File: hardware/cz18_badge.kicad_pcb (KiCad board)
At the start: 2 copper layers, 91.5 x 99.6 mm, 37 parts, among them J1 Dev breakout (opt.), J2 VCC (max 5V), J3 GND, J4 LEDS OUT, SW1 MODE, SW2 SLOT, SW3 LEARN, SW4 PLAY, U1 CHQ1838, U2 NRF24L01 (opt.)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

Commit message: Finished annotation
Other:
- board text added: "D2"
- board text added: "D3"
- board text added: "D4"
- board text added: "D5"
- board text added: "D6"
- board text added: "RX"
- board text added: "TX"
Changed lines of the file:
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@@
     (links 119)
     (no_connects 119)
-    (area 86.149249 48.166589 177.749413 147.831598)
+    (area 79.807143 32.561796 178.694531 147.831598)
     (thickness 1.6)
-    (drawings 421)
+    (drawings 430)
     (tracks 0)
     (zones 0)
@@
     (35 F.Paste user)
     (36 B.SilkS user)
-    (37 F.SilkS user)
+    (37 F.SilkS user hide)
     (38 B.Mask user)
     (39 F.Mask user)
@@
     (pad 1 thru_hole circle (at 2.280419 -2.280419) (size 0.9 0.9) (drill 0.6) (layers *.Cu *.Mask))
   )
+  (gr_text TX (at 169.5 86.5 10) (layer B.SilkS)
+    (effects (font (size 1 1) (thickness 0.15)) (justify mirror))
+  )
+  (gr_text RX (at 170 89 10) (layer B.SilkS)
+    (effects (font (size 1 1) (thickness 0.15)) (justify mirror))
+  )
+  (gr_text RST (at 170.5 91.5 10) (layer B.SilkS)
+    (effects (font (size 1 1) (thickness 0.15)) (justify mirror))
+  )
+  (gr_text GND (at 171 94 10) (layer B.SilkS)
+    (effects (font (size 1 1) (thickness 0.15)) (justify mirror))
+  )
+  (gr_text D2 (at 171 96.5 10) (layer B.SilkS)
+    (effects (font (size 1 1) (thickness 0.15)) (justify mirror))
+  )
+  (gr_text D3 (at 171.5 99 10) (layer B.SilkS)
+    (effects (font (size 1 1) (thickness 0.15)) (justify mirror))
+  )
+  (gr_text D4 (at 172 101.5 10) (layer B.SilkS)
+    (effects (font (size 1 1) (thickness 0.15)) (justify mirror))
+  )
+  (gr_text D5 (at 172.5 104 10) (layer B.SilkS)
+    (effects (font (size 1 1) (thickness 0.15)) (justify mirror))
+  )
+  (gr_text D6 (at 173 106.5 10) (layer B.SilkS)
+    (effects (font (size 1 1) (thickness 0.15)) (justify mirror))
+  )
   (gr_text D7 (at 173.5 109 10) (layer B.SilkS)

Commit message: Added minimal track widths and clearances for JLCPCB
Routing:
- added copper zone on B.Cu, net VCC
- added copper zone on F.Cu, net VCC
- removed copper zone on B.Cu, net GND
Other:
- net class Default: clearance 0.25 -> 0.127; trace_width 0.25 -> 0.127
- net class Power added: clearance 0.25, trace_width 0.25, via_dia 0.6, via_drill 0.4
- rule trace_clearance: 0.25 -> 0.127
- rule trace_min: 0.2 -> 0.127
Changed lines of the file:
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@@
     (35 F.Paste user)
     (36 B.SilkS user)
-    (37 F.SilkS user hide)
+    (37 F.SilkS user)
     (38 B.Mask user)
     (39 F.Mask user)
@@
   )
   (setup
-    (last_trace_width 0.25)
-    (trace_clearance 0.25)
-    (zone_clearance 0.508)
+    (last_trace_width 0.127)
+    (trace_clearance 0.127)
+    (zone_clearance 0.2)
     (zone_45_only no)
-    (trace_min 0.2)
+    (trace_min 0.127)
     (segment_width 0.25)
     (edge_width 0.15)
@@
   (net 34 "Net-(U2-Pad8)")
   (net_class Default "This is the default net class."
-    (clearance 0.25)
-    (trace_width 0.25)
+    (clearance 0.127)
+    (trace_width 0.127)
     (via_dia 0.6)
     (via_drill 0.4)
     (uvia_dia 0.3)
     (uvia_drill 0.1)
-    (add_net 3V3)
     (add_net A0)
     (add_net A1)
@@
     (add_net A6)
     (add_net A7)
-    (add_net AREF)
     (add_net BUZZ1)
     (add_net BUZZ2)
@@
     (add_net D7)
     (add_net D8)
-    (add_net GND)
     (add_net "Net-(D1-Pad4)")
     (add_net "Net-(D2-Pad4)")
@@
     (add_net RX)
     (add_net TX)
+  )
+  (net_class Power ""
+    (clearance 0.25)
+    (trace_width 0.25)
+    (via_dia 0.6)
+    (via_drill 0.4)
+    (uvia_dia 0.3)
+    (uvia_drill 0.1)
+    (add_net 3V3)
+    (add_net AREF)
+    (add_net GND)
     (add_net VCC)
     (add_net VIN)
@@
   (gr_line (start 164.777843 140.94158) (end 161.054639 143.439932) (layer Edge.Cuts) (width 0.1))
   (gr_line (start 166.819753 139.21182) (end 164.777843 140.94158) (layer Edge.Cuts) (width 0.1))
-  (zone (net 15) (net_name GND) (layer F.Cu) (hatch full 0.508)
+  (zone (net 3) (net_name VCC) (layer F.Cu) (hatch full 0.508)
     (connect_pads (clearance 0.808))
     (min_thickness 0.254)
@@
     )
   )
-  (zone (net 15) (net_name GND) (layer F.Cu) (hatch full 0.508)
+  (zone (net 3) (net_name VCC) (layer F.Cu) (hatch full 0.508)
     (connect_pads (clearance 0.808))
     (min_thickness 0.254)
@@
     )
   )
-  (zone (net 15) (net_name GND) (layer F.Cu) (hatch full 0.508)
+  (zone (net 3) (net_name VCC) (layer F.Cu) (hatch full 0.508)
     (connect_pads (clearance 0.808))
     (min_thickness 0.254)
@@
     )
   )
-  (zone (net 15) (net_name GND) (layer F.Cu) (hatch full 0.508)
+  (zone (net 3) (net_name VCC) (layer F.Cu) (hatch full 0.508)
     (connect_pads (clearance 0.808))
     (min_thickness 0.254)
@@
     )
   )
-  (zone (net 15) (net_name GND) (layer F.Cu) (hatch full 0.508)
-    (connect_pads (clearance 0.808))
-    (min_thickness 0.254)
-    (fill (arc_segments 16) (thermal_gap 0.508) (thermal_bridge_width 0.508))
+  (zone (net 3) (net_name VCC) (layer F.Cu) (hatch full 0.508)
+    (connect_pads (clearance 0.2))
+    (min_thickness 0.127)
+    (fill (arc_segments 16) (thermal_gap 0.2) (thermal_bridge_width 0.508))
     (polygon
       (pts
@@
     )
   )
-  (zone (net 15) (net_name GND) (layer F.Cu) (hatch full 0.508)
-    (connect_pads (clearance 0.508))
-    (min_thickness 0.254)
-    (fill (arc_segments 16) (thermal_gap 0.508) (thermal_bridge_width 0.508))
+  (zone (net 3) (net_name VCC) (layer F.Cu) (hatch full 0.508)
+    (connect_pads (clearance 0.2))
+    (min_thickness 0.127)
+    (fill (arc_segments 16) (thermal_gap 0.2) (thermal_bridge_width 0.508))
     (polygon
       (pts
@@
     )
   )
-  (zone (net 15) (net_name GND) (layer F.Cu) (hatch full 0.508)
-    (connect_pads (clearance 0.508))
-    (min_thickness 0.254)
-    (fill (arc_segments 16) (thermal_gap 0.508) (thermal_bridge_width 0.508))
+  (zone (net 3) (net_name VCC) (layer F.Cu) (hatch full 0.508)
+    (connect_pads (clearance 0.2))
+    (min_thickness 0.127)
+    (fill (arc_segments 16) (thermal_gap 0.2) (thermal_bridge_width 0.508))
     (polygon
       (pts
@@
     )
   )
-  (zone (net 15) (net_name GND) (layer F.Cu) (hatch full 0.508)
-    (connect_pads (clearance 0.508))
-    (min_thickness 0.254)
-    (fill (arc_segments 16) (thermal_gap 0.508) (thermal_bridge_width 0.508))
+  (zone (net 3) (net_name VCC) (layer F.Cu) (hatch full 0.508)
+    (connect_pads (clearance 0.2))
+    (min_thickness 0.127)
+    (fill (arc_segments 16) (thermal_gap 0.2) (thermal_bridge_width 0.508))
     (polygon
       (pts
@@
     )
   )
-  (zone (net 15) (net_name GND) (layer F.Cu) (hatch full 0.508)
-    (connect_pads (clearance 0.508))
-    (min_thickness 0.254)
-    (fill (arc_segments 16) (thermal_gap 0.508) (thermal_bridge_width 0.508))
+  (zone (net 3) (net_name VCC) (layer F.Cu) (hatch full 0.508)
+    (connect_pads (clearance 0.2))
+    (min_thickness 0.127)
+    (fill (arc_segments 16) (thermal_gap 0.2) (thermal_bridge_width 0.508))
     (polygon
       (pts
@@
     )
   )
-  (zone (net 15) (net_name GND) (layer F.Cu) (hatch full 0.508)
-    (connect_pads (clearance 0.808))
-    (min_thickness 0.254)
-    (fill (arc_segments 16) (thermal_gap 0.508) (thermal_bridge_width 0.508))
+  (zone (net 3) (net_name VCC) (layer F.Cu) (hatch full 0.508)
+    (connect_pads (clearance 0.2))
+    (min_thickness 0.127)
+    (fill (arc_segments 16) (thermal_gap 0.2) (thermal_bridge_width 0.508))
     (polygon
       (pts
@@
     )
   )
-  (zone (net 15) (net_name GND) (layer F.Cu) (hatch full 0.508)
-    (connect_pads (clearance 0.808))
-    (min_thickness 0.254)
-    (fill (arc_segments 16) (thermal_gap 0.508) (thermal_bridge_width 0.508))
+  (zone (net 3) (net_name VCC) (layer F.Cu) (hatch full 0.508)
+    (connect_pads (clearance 0.2))
+    (min_thickness 0.127)
+    (fill (arc_segments 16) (thermal_gap 0.2) (thermal_bridge_width 0.508))
     (polygon
       (pts
@@
   )
   (zone (net 15) (net_name GND) (layer F.Cu) (hatch full 0.508)
-    (connect_pads (clearance 0.808))
-    (min_thickness 0.254)
-    (fill (arc_segments 16) (thermal_gap 0.508) (thermal_bridge_width 0.508))
+    (connect_pads (clearance 0.2))
+    (min_thickness 0.127)
+    (fill (arc_segments 16) (thermal_gap 0.2) (thermal_bridge_width 0.508))
     (polygon
       (pts
@@
     )
   )
-  (zone (net 15) (net_name GND) (layer F.Cu) (hatch full 0.508)
-    (connect_pads (clearance 0.808))
-    (min_thickness 0.254)
-    (fill (arc_segments 16) (thermal_gap 0.508) (thermal_bridge_width 0.508))
+  (zone (net 3) (net_name VCC) (layer F.Cu) (hatch full 0.508)
+    (connect_pads (clearance 0.2))
+    (min_thickness 0.127)
+    (fill (arc_segments 16) (thermal_gap 0.2) (thermal_bridge_width 0.508))
     (polygon
       (pts
@@
     )
   )
-  (zone (net 15) (net_name GND) (layer B.Cu) (hatch full 0.508)
-    (connect_pads (clearance 0.508))
-    (min_thickness 0.254)
-    (fill (arc_segments 16) (thermal_gap 0.508) (thermal_bridge_width 0.508))
+  (zone (net 3) (net_name VCC) (layer B.Cu) (hatch full 0.508)
+    (connect_pads (clearance 0.2))
+    (min_thickness 0.127)
+    (fill (arc_segments 16) (thermal_gap 0.2) (thermal_bridge_width 0.508))
     (polygon
       (pts

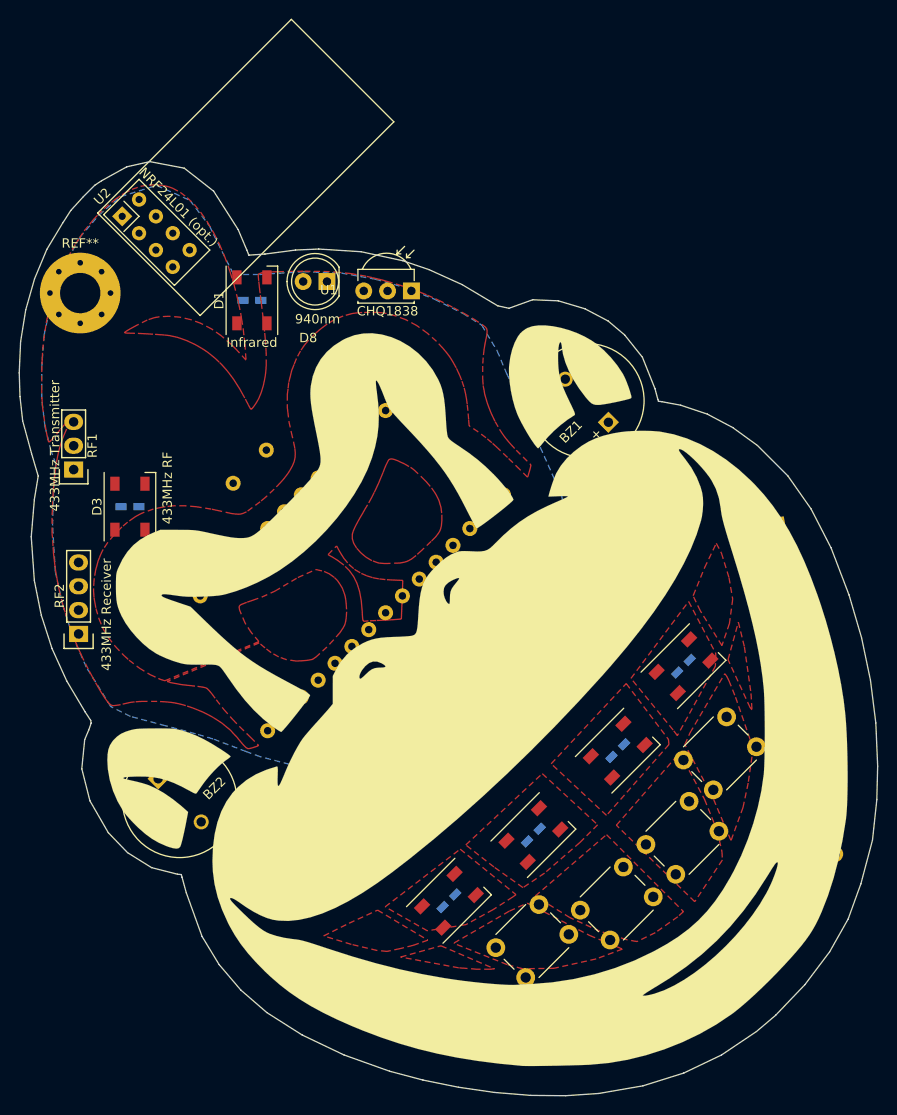
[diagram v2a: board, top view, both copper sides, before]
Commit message: Performed Autoroute, still 14 connections missing.
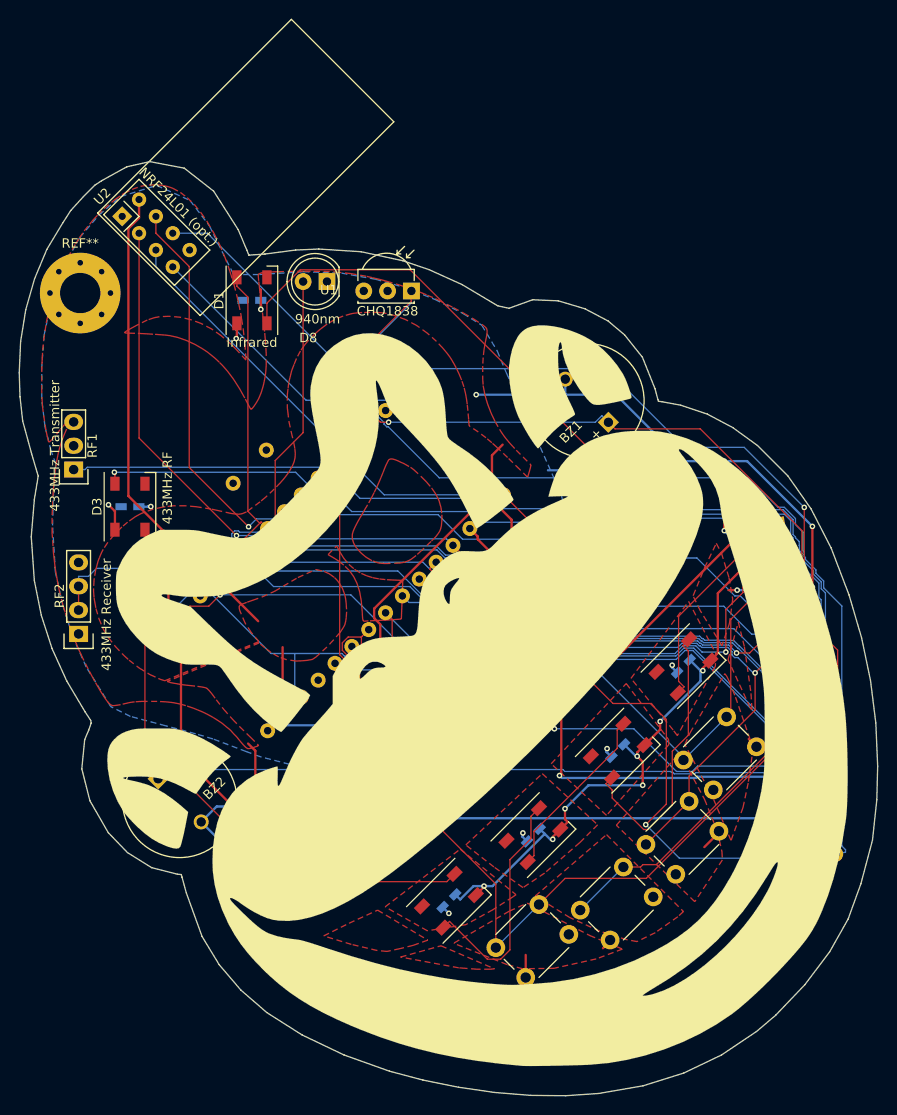
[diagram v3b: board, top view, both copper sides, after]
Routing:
- net GND: track 0.00 -> 196.3 mm, vias 0 -> 17
- net 3V3: track 0.00 -> 185.4 mm
- net D11: track 0.00 -> 122.6 mm, vias 0 -> 1
- net A0: track 0.00 -> 121.0 mm, vias 0 -> 2
- net D12: track 0.00 -> 120.5 mm
- net D13: track 0.00 -> 114.3 mm, vias 0 -> 1
- net BUZZ2: track 0.00 -> 114.2 mm, vias 0 -> 1
- net A1: track 0.00 -> 110.9 mm, vias 0 -> 2
- net D7: track 0.00 -> 109.6 mm
- net D8: track 0.00 -> 108.2 mm
- net D4: track 0.00 -> 97.8 mm, vias 0 -> 1
- net D3: track 0.00 -> 94.7 mm
- net BUZZ1: track 0.00 -> 87.8 mm, vias 0 -> 1
- net A5: track 0.00 -> 86.9 mm, vias 0 -> 1
- net D2: track 0.00 -> 85.3 mm, vias 0 -> 1
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
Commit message: Completed final manual routing
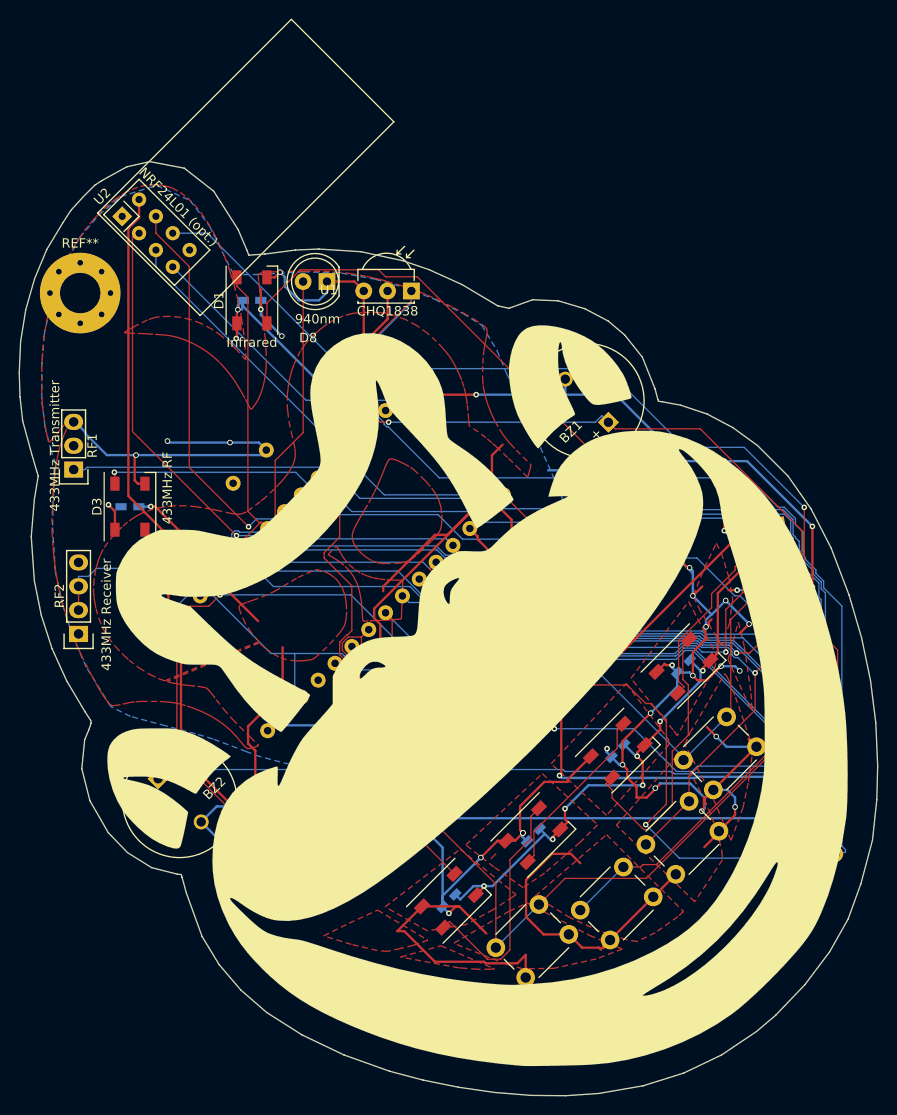
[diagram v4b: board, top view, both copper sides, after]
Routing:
- net VCC: track 36.0 -> 283.2 mm, vias 8 -> 28
- net GND: track 196.3 -> 292.9 mm, vias 17 -> 24
- net 3V3: track 185.4 -> 197.8 mm
- net Net-(D3-Pad4): track 62.1 -> 67.0 mm
- net BUZZ2: track 114.2 -> 116.7 mm
- net A1: track 110.9 -> 111.7 mm
- net (no net): track 0.00 -> 0.71 mm
- added copper zone on F.Cu, net 3V3

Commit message: Added eye shade fill zones again, and performed final modifications to tracks. Generated gerber files.
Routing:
- net GND: track 292.9 -> 318.1 mm
- net VCC: track 283.2 -> 294.4 mm
- net 3V3: track 197.8 -> 188.2 mm
- net D11: track 122.6 -> 121.8 mm
- net (no net): track 0.71 -> 0.00 mm
- removed copper zone on F.Cu, net 3V3
